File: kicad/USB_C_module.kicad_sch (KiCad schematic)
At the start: 1 part, among them J3 USB4110-GF-A

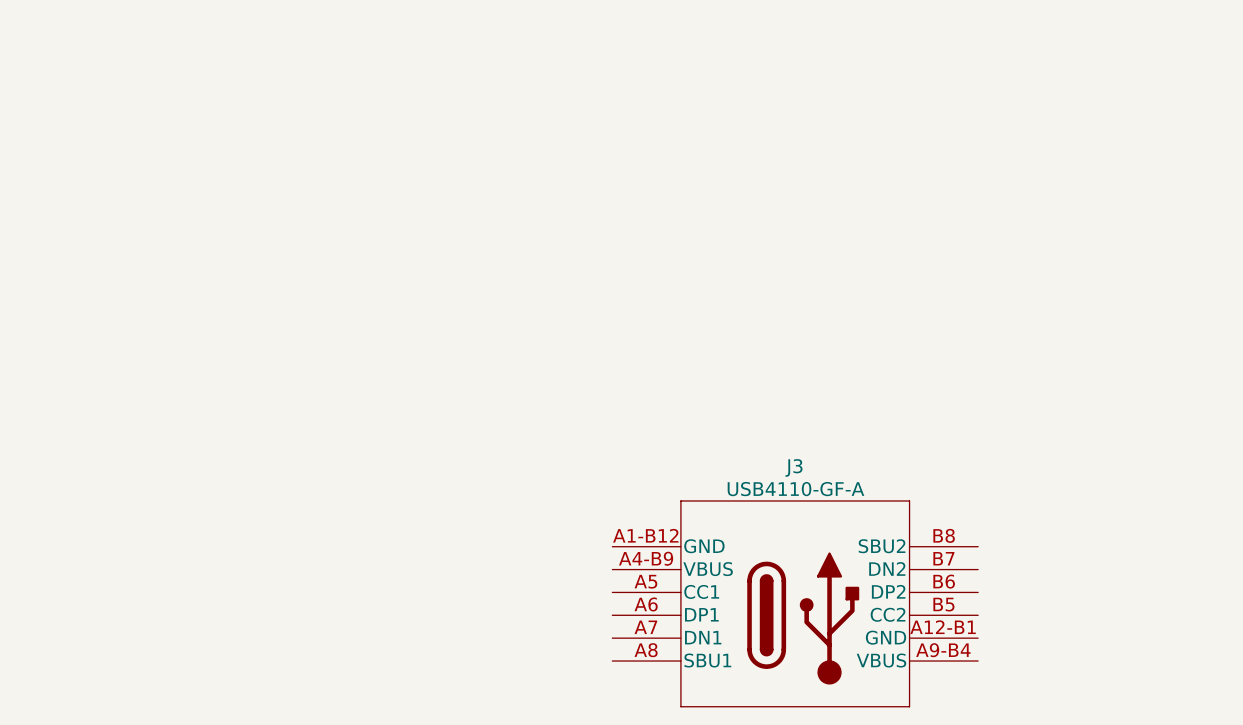
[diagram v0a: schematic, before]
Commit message: Updated USB module
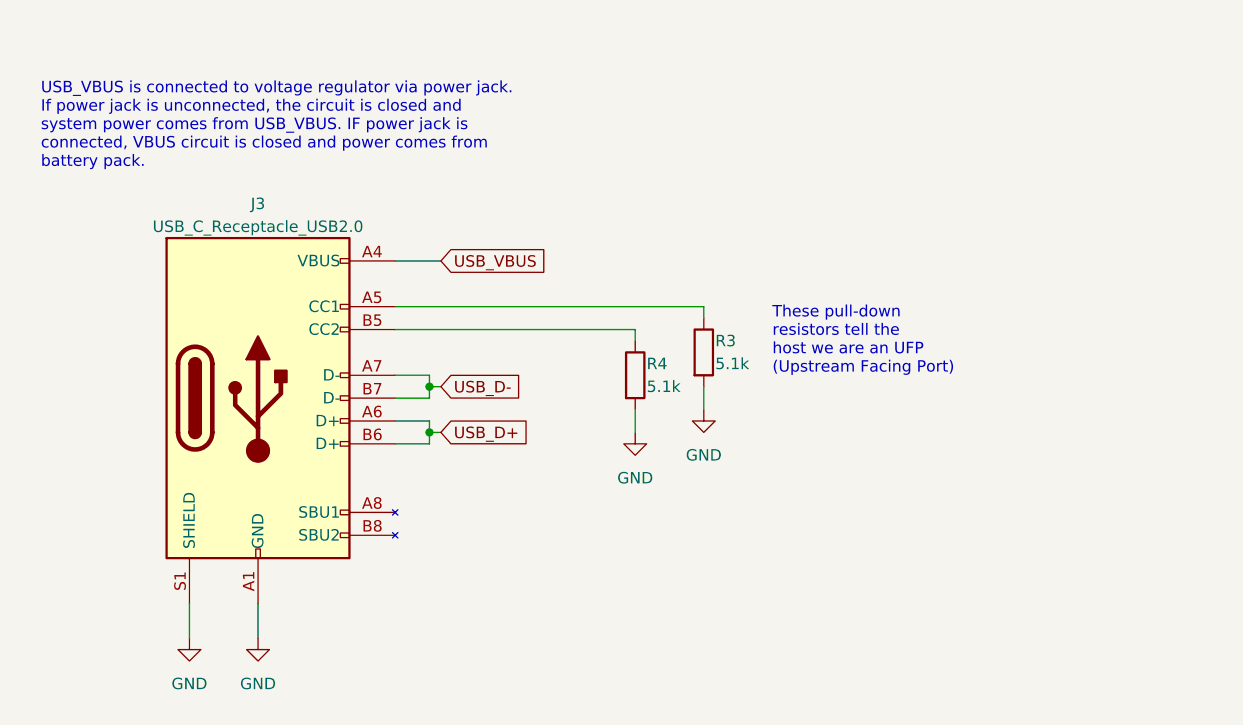
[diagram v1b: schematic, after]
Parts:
- removed J3: USB4110-GF-A, USB4110-GF-A_GCT, symbol USB4110-GF-A:USB4110-GF-A
- added J3: USB_C_Receptacle_USB2.0, symbol Connector:USB_C_Receptacle_USB2.0
- added R3, R4: 5.1k, symbol Device:R
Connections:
- new net: J3.A5 (CC1), R3.1
- new net: J3.B5 (CC2), R4.1
- new net GND: J3.A1 (GND), J3.A12 (GND), J3.B1 (GND), J3.B12 (GND), J3.S1 (SHIELD), R3.2, R4.2
- new net USB_D+: J3.A6 (D+), J3.B6 (D+)
- new net USB_D-: J3.A7 (D-), J3.B7 (D-)
- new net USB_VBUS: J3.A4 (VBUS), J3.A9 (VBUS), J3.B4 (VBUS), J3.B9 (VBUS)
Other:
- note added: "These pull-down resistors tell the host we are an UFP (Upstream Facing Port)"
- note added: "USB_VBUS is connected to voltage regulator via power jack. If power jack is unconnected, the circuit is closed and system power comes from USB_VBUS. IF power jack is connected, VBUS circuit is closed and power comes from battery pack."
- company: (none) -> University of Oulu
- title: (none) -> USB-C module

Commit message: voltage regulator update
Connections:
- net GND: no longer J3.A1 (GND), J3.A12 (GND), J3.B1 (GND), J3.B12 (GND)
- new net USB_GND: J3.A1 (GND), J3.A12 (GND), J3.B1 (GND), J3.B12 (GND)
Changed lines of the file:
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@@
     (stroke (width 0) (type default))
   )
-  (wire (pts (xy 67.31 87.63) (xy 67.31 91.44))
+  (wire (pts (xy 67.31 87.63) (xy 67.31 93.98))
     (stroke (width 0) (type default))
   )
@@
   )
   (wire (pts (xy 86.36 64.77) (xy 86.36 63.5))
+    (stroke (width 0) (type default))
+  )
+  (wire (pts (xy 67.31 93.98) (xy 72.39 93.98))
     (stroke (width 0) (type default))
   )
@@
     (effects (font (size 1.27 1.27)) (justify left))
     (property "Intersheetrefs" "${INTERSHEET_REFS}" (at 98.1558 63.5 0)
+      (effects (font (size 1.27 1.27)) (justify left) hide)
+    )
+  )
+  (global_label "USB_GND" (shape input) (at 72.39 93.98 0) (fields_autoplaced)
+    (effects (font (size 1.27 1.27)) (justify left))
+    (property "Intersheetrefs" "${INTERSHEET_REFS}" (at 83.9439 93.98 0)
       (effects (font (size 1.27 1.27)) (justify left) hide)
     )
@@
         )
       )
-    )
-  )
-  (symbol (lib_id "power:GND") (at 67.31 91.44 0) (unit 1)
-    (in_bom yes) (on_board yes) (dnp no) (fields_autoplaced)
-    (property "Reference" "#PWR019" (at 67.31 97.79 0)
-      (effects (font (size 1.27 1.27)) hide)
-    )
-    (property "Value" "GND" (at 67.31 96.52 0)
-      (effects (font (size 1.27 1.27)))
-    )
-    (property "Footprint" "" (at 67.31 91.44 0)
-      (effects (font (size 1.27 1.27)) hide)
-    )
-    (property "Datasheet" "" (at 67.31 91.44 0)
-      (effects (font (size 1.27 1.27)) hide)
-    )
-    (pin "1")
-    (instances
-      (project "IoT_sulari"
-        (path "/184b47ed-2c2b-4c02-be35-d18f4f4e5685/a70bd09f-d983-47ca-8017-0524420ada83"
-          (reference "#PWR019") (unit 1)
-        )
-      )

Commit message: added status leds
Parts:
- added U6: TPD2E2U06DCKR, DCK0003A-IPC_A, symbol TPD2E2U06DCKR:TPD2E2U06DCKR
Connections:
- net GND: now also U6.3 (GND)
- net USB_D+: now also U6.2 (IO2)
- net USB_D-: now also U6.1 (IO1)
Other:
- moved on the sheet: J3, R3, R4

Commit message: added comments and muokkasin komponenttiennumeroinnin selvemmäksi.
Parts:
- renumbered J3 to J50, R4 to R50, R3 to R51, U6 to U50
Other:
- note added: "ESD protector is needed to protect MCU from ESD shock."
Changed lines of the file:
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@@
+    (effects (font (size 1.27 1.27)) (justify left bottom))
+  )
+  (text "ESD protector is needed to protect\nMCU from ESD shock."
+    (at 91.44 93.98 0)
     (effects (font (size 1.27 1.27)) (justify left bottom))
   )
@@
   (symbol (lib_id "Connector:USB_C_Receptacle_USB2.0") (at 64.77 58.42 0) (unit 1)
     (in_bom yes) (on_board yes) (dnp no) (fields_autoplaced)
-    (property "Reference" "J3" (at 64.77 36.83 0)
+    (property "Reference" "J50" (at 64.77 36.83 0)
       (effects (font (size 1.27 1.27)))
     )
@@
       (project "IoT_sulari"
         (path "/184b47ed-2c2b-4c02-be35-d18f4f4e5685/a70bd09f-d983-47ca-8017-0524420ada83"
-          (reference "J3") (unit 1)
+          (reference "J50") (unit 1)
         )
       )
@@
   (symbol (lib_id "Device:R") (at 139.7 53.34 0) (unit 1)
     (in_bom yes) (on_board yes) (dnp no)
-    (property "Reference" "R3" (at 140.97 52.07 0)
+    (property "Reference" "R51" (at 140.97 52.07 0)
       (effects (font (size 1.27 1.27)) (justify left))
     )
@@
       (project "IoT_sulari"
         (path "/184b47ed-2c2b-4c02-be35-d18f4f4e5685/a70bd09f-d983-47ca-8017-0524420ada83"
-          (reference "R3") (unit 1)
+          (reference "R51") (unit 1)
         )
       )
@@
   (symbol (lib_id "TPD2E2U06DCKR:TPD2E2U06DCKR") (at 95.25 77.47 0) (unit 1)
     (in_bom yes) (on_board yes) (dnp no) (fields_autoplaced)
-    (property "Reference" "U6" (at 110.49 68.58 0)
+    (property "Reference" "U50" (at 110.49 68.58 0)
       (effects (font (size 1.524 1.524)))
     )
@@
       (project "IoT_sulari"
         (path "/184b47ed-2c2b-4c02-be35-d18f4f4e5685/a70bd09f-d983-47ca-8017-0524420ada83"
-          (reference "U6") (unit 1)
+          (reference "U50") (unit 1)
         )
       )
@@
   (symbol (lib_id "Device:R") (at 132.08 55.88 0) (unit 1)
     (in_bom yes) (on_board yes) (dnp no)
-    (property "Reference" "R4" (at 133.35 54.61 0)
+    (property "Reference" "R50" (at 133.35 54.61 0)
       (effects (font (size 1.27 1.27)) (justify left))
     )
@@
       (project "IoT_sulari"
         (path "/184b47ed-2c2b-4c02-be35-d18f4f4e5685/a70bd09f-d983-47ca-8017-0524420ada83"
-          (reference "R4") (unit 1)
-        )
-      )
+          (reference "R50") (unit 1)
+        )
+      )

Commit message: USB-module delete
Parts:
- removed J50: USB_C_Receptacle_USB2.0, symbol Connector:USB_C_Receptacle_USB2.0
- removed R50, R51: 5.1k, symbol Device:R
- removed U50: TPD2E2U06DCKR, DCK0003A-IPC_A, symbol TPD2E2U06DCKR:TPD2E2U06DCKR
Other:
- note removed: "ESD protector is needed to protect MCU from ESD shock."
- note removed: "These pull-down resistors tell the host we are an UFP (Upstream Facing Port)"
- note removed: "USB_VBUS is connected to voltage regulator via power jack. If power jack is unconnected, the circuit is closed and system power comes from USB_VBUS. IF power jack is connected, VBUS circuit is closed and power comes from battery pack."
- company: University of Oulu -> (none)
- title: USB-C module -> (none)
